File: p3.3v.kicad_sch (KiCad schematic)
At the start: 11 parts, among them U11 LT3045xDD

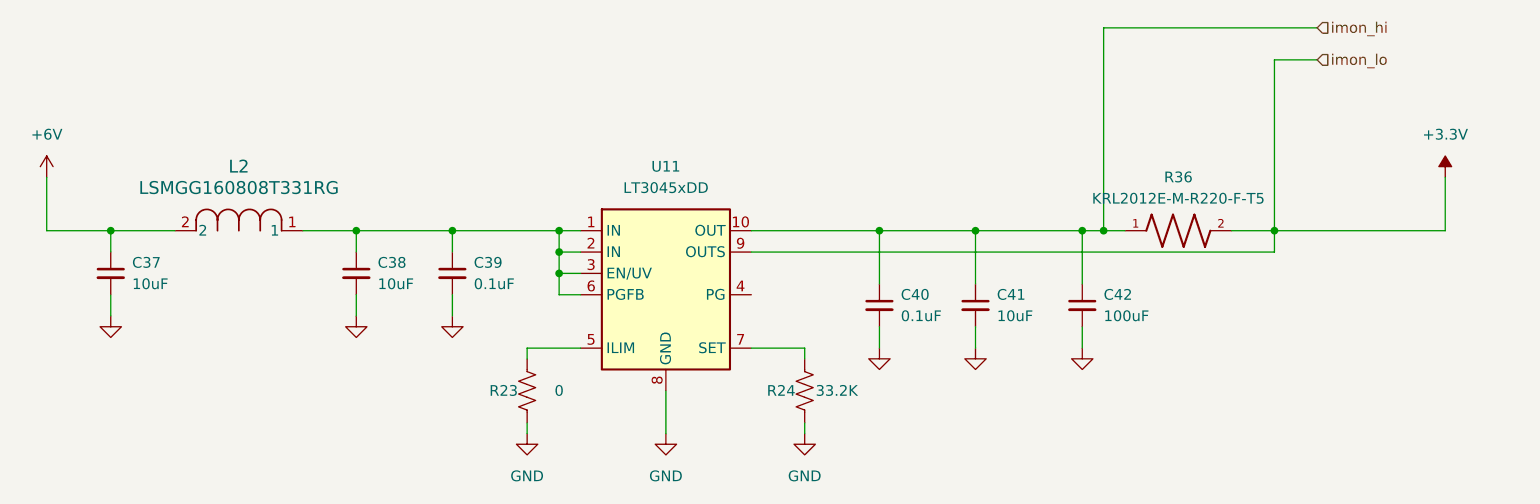
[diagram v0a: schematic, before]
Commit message: Add all 4 channels
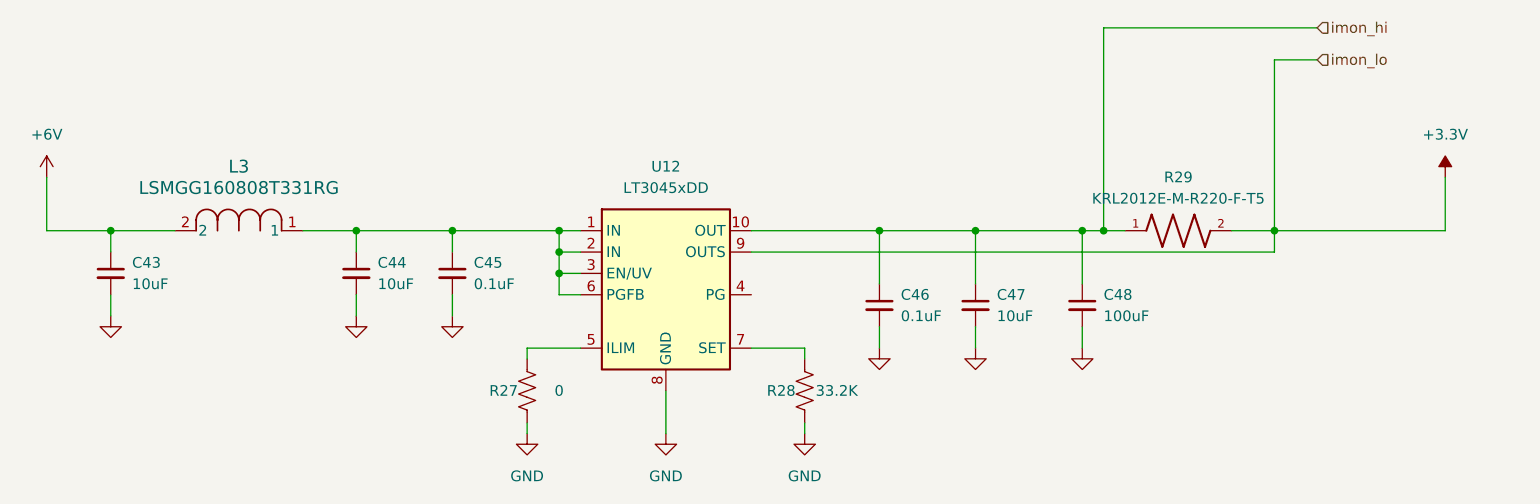
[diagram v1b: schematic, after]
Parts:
- renumbered C37 to C43, C38 to C44, C39 to C45, C40 to C46, C41 to C47, C42 to C48, L2 to L3, R23 to R27, R24 to R28, R36 to R29, U11 to U12
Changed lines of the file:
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@@
 		(dnp no)
 		(fields_autoplaced yes)
-		(property "Reference" "#PWR097"
+		(property "Reference" "#PWR0113"
 			(at 181.61 91.44 0)
 			(effects
@@
 			(project "psc_carrier_brd"
 				(path "/40891cc8-bf64-41f4-8f69-a607d7b280eb/d1842e08-6ad7-4891-bdb3-3a3a498e2a30/81cf0a5d-1890-4a8a-965e-c38ae4a2ca5e"
-					(reference "#PWR097")
+					(reference "#PWR0113")
 					(unit 1)
 				)
@@
 		(dnp no)
 		(fields_autoplaced yes)
-		(property "Reference" "#PWR099"
+		(property "Reference" "#PWR0115"
 			(at 237.49 68.58 0)
 			(effects
@@
 			(project ""
 				(path "/40891cc8-bf64-41f4-8f69-a607d7b280eb/d1842e08-6ad7-4891-bdb3-3a3a498e2a30/81cf0a5d-1890-4a8a-965e-c38ae4a2ca5e"
-					(reference "#PWR099")
+					(reference "#PWR0115")
 					(unit 1)
 				)
@@
 		(dnp no)
 		(fields_autoplaced yes)
-		(property "Reference" "#PWR090"
+		(property "Reference" "#PWR0106"
 			(at 78.74 87.63 0)
 			(effects
@@
 			(project "psc_carrier_brd"
 				(path "/40891cc8-bf64-41f4-8f69-a607d7b280eb/d1842e08-6ad7-4891-bdb3-3a3a498e2a30/81cf0a5d-1890-4a8a-965e-c38ae4a2ca5e"
-					(reference "#PWR090")
+					(reference "#PWR0106")
 					(unit 1)
 				)
@@
 		(on_board yes)
 		(dnp no)
-		(property "Reference" "R23"
+		(property "Reference" "R27"
 			(at 125.476 90.17 0)
 			(effects
@@
 			(project "psc_carrier_brd"
 				(path "/40891cc8-bf64-41f4-8f69-a607d7b280eb/d1842e08-6ad7-4891-bdb3-3a3a498e2a30/81cf0a5d-1890-4a8a-965e-c38ae4a2ca5e"
-					(reference "R23")
+					(reference "R27")
 					(unit 1)
 				)
@@
 		(on_board yes)
 		(dnp no)
-		(property "Reference" "C37"
+		(property "Reference" "C43"
 			(at 81.28 74.9362 0)
 			(effects
@@
 			(project "psc_carrier_brd"
 				(path "/40891cc8-bf64-41f4-8f69-a607d7b280eb/d1842e08-6ad7-4891-bdb3-3a3a498e2a30/81cf0a5d-1890-4a8a-965e-c38ae4a2ca5e"
-					(reference "C37")
+					(reference "C43")
 					(unit 1)
 				)
@@
 		(on_board yes)
 		(dnp no)
-		(property "Reference" "C39"
+		(property "Reference" "C45"
 			(at 121.92 74.9362 0)
 			(effects
@@
 			(project "psc_carrier_brd"
 				(path "/40891cc8-bf64-41f4-8f69-a607d7b280eb/d1842e08-6ad7-4891-bdb3-3a3a498e2a30/81cf0a5d-1890-4a8a-965e-c38ae4a2ca5e"
-					(reference "C39")
+					(reference "C45")
 					(unit 1)
 				)
@@
 		(dnp no)
 		(fields_autoplaced yes)
-		(property "Reference" "#PWR092"
+		(property "Reference" "#PWR0108"
 			(at 119.38 87.63 0)
 			(effects
@@
 			(project "psc_carrier_brd"
 				(path "/40891cc8-bf64-41f4-8f69-a607d7b280eb/d1842e08-6ad7-4891-bdb3-3a3a498e2a30/81cf0a5d-1890-4a8a-965e-c38ae4a2ca5e"
-					(reference "#PWR092")
+					(reference "#PWR0108")
 					(unit 1)
 				)
@@
 		(on_board yes)
 		(dnp no)
-		(property "Reference" "C42"
+		(property "Reference" "C48"
 			(at 196.85 78.7462 0)
 			(effects
@@
 			(project "psc_carrier_brd"
 				(path "/40891cc8-bf64-41f4-8f69-a607d7b280eb/d1842e08-6ad7-4891-bdb3-3a3a498e2a30/81cf0a5d-1890-4a8a-965e-c38ae4a2ca5e"
-					(reference "C42")
+					(reference "C48")
 					(unit 1)
 				)
@@
 		(on_board yes)
 		(dnp no)
-		(property "Reference" "R24"
+		(property "Reference" "R28"
 			(at 158.496 90.17 0)
 			(effects
@@
 			(project "psc_carrier_brd"
 				(path "/40891cc8-bf64-41f4-8f69-a607d7b280eb/d1842e08-6ad7-4891-bdb3-3a3a498e2a30/81cf0a5d-1890-4a8a-965e-c38ae4a2ca5e"
-					(reference "R24")
+					(reference "R28")
 					(unit 1)
 				)
@@
 		(dnp no)
 		(fields_autoplaced yes)
-		(property "Reference" "#PWR096"
+		(property "Reference" "#PWR0112"
 			(at 170.18 91.44 0)
 			(effects
@@
 			(project "psc_carrier_brd"
 				(path "/40891cc8-bf64-41f4-8f69-a607d7b280eb/d1842e08-6ad7-4891-bdb3-3a3a498e2a30/81cf0a5d-1890-4a8a-965e-c38ae4a2ca5e"
-					(reference "#PWR096")
+					(reference "#PWR0112")
 					(unit 1)
 				)
@@
 		(dnp no)
 		(fields_autoplaced yes)
-		(property "Reference" "#PWR095"
+		(property "Reference" "#PWR0111"
 			(at 161.29 101.6 0)
 			(effects
@@
 			(project "psc_carrier_brd"
 				(path "/40891cc8-bf64-41f4-8f69-a607d7b280eb/d1842e08-6ad7-4891-bdb3-3a3a498e2a30/81cf0a5d-1890-4a8a-965e-c38ae4a2ca5e"
-					(reference "#PWR095")
+					(reference "#PWR0111")
 					(unit 1)
 				)
@@
 		(dnp no)
 		(fields_autoplaced yes)
-		(property "Reference" "#PWR091"
+		(property "Reference" "#PWR0107"
 			(at 107.95 87.63 0)
 			(effects
@@
 			(project "psc_carrier_brd"
 				(path "/40891cc8-bf64-41f4-8f69-a607d7b280eb/d1842e08-6ad7-4891-bdb3-3a3a498e2a30/81cf0a5d-1890-4a8a-965e-c38ae4a2ca5e"
-					(reference "#PWR091")
+					(reference "#PWR0107")
 					(unit 1)
 				)
@@
 		(on_board yes)
 		(dnp no)
-		(property "Reference" "C38"
+		(property "Reference" "C44"
 			(at 110.49 74.9362 0)
 			(effects
@@
 			(project "psc_carrier_brd"
 				(path "/40891cc8-bf64-41f4-8f69-a607d7b280eb/d1842e08-6ad7-4891-bdb3-3a3a498e2a30/81cf0a5d-1890-4a8a-965e-c38ae4a2ca5e"
-					(reference "C38")
+					(reference "C44")
 					(unit 1)
 				)
@@
 		(dnp no)
 		(fields_autoplaced yes)
-		(property "Reference" "#PWR093"
+		(property "Reference" "#PWR0109"
 			(at 128.27 101.6 0)
 			(effects
@@
 			(project "psc_carrier_brd"
 				(path "/40891cc8-bf64-41f4-8f69-a607d7b280eb/d1842e08-6ad7-4891-bdb3-3a3a498e2a30/81cf0a5d-1890-4a8a-965e-c38ae4a2ca5e"
-					(reference "#PWR093")
+					(reference "#PWR0109")
 					(unit 1)
 				)
@@
 		(dnp no)
 		(fields_autoplaced yes)
-		(property "Reference" "R36"
+		(property "Reference" "R29"
 			(at 205.74 64.77 0)
 			(effects
@@
 			(project "psc_carrier_brd"
 				(path "/40891cc8-bf64-41f4-8f69-a607d7b280eb/d1842e08-6ad7-4891-bdb3-3a3a498e2a30/81cf0a5d-1890-4a8a-965e-c38ae4a2ca5e"
-					(reference "R36")
+					(reference "R29")
 					(unit 1)
 				)
@@
 		(dnp no)
 		(fields_autoplaced yes)
-		(property "Reference" "#PWR098"
+		(property "Reference" "#PWR0114"
 			(at 194.31 91.44 0)
 			(effects
@@
 			(project "psc_carrier_brd"
 				(path "/40891cc8-bf64-41f4-8f69-a607d7b280eb/d1842e08-6ad7-4891-bdb3-3a3a498e2a30/81cf0a5d-1890-4a8a-965e-c38ae4a2ca5e"
-					(reference "#PWR098")
+					(reference "#PWR0114")
 					(unit 1)
 				)
@@
 		(on_board yes)
 		(dnp no)
-		(property "Reference" "C40"
+		(property "Reference" "C46"
 			(at 172.72 78.7462 0)
 			(effects
@@
 			(project "psc_carrier_brd"
 				(path "/40891cc8-bf64-41f4-8f69-a607d7b280eb/d1842e08-6ad7-4891-bdb3-3a3a498e2a30/81cf0a5d-1890-4a8a-965e-c38ae4a2ca5e"
-					(reference "C40")
+					(reference "C46")
 					(unit 1)
 				)
@@
 		(dnp no)
 		(fields_autoplaced yes)
-		(property "Reference" "#PWR094"
+		(property "Reference" "#PWR0110"
 			(at 144.78 101.6 0)
 			(effects
@@
 			(project ""
 				(path "/40891cc8-bf64-41f4-8f69-a607d7b280eb/d1842e08-6ad7-4891-bdb3-3a3a498e2a30/81cf0a5d-1890-4a8a-965e-c38ae4a2ca5e"
-					(reference "#PWR094")
+					(reference "#PWR0110")
 					(unit 1)
 				)
@@
 		(dnp no)
 		(fields_autoplaced yes)
-		(property "Reference" "U11"
+		(property "Reference" "U12"
 			(at 144.78 63.5 0)
 			(effects
@@
 			(project ""
 				(path "/40891cc8-bf64-41f4-8f69-a607d7b280eb/d1842e08-6ad7-4891-bdb3-3a3a498e2a30/81cf0a5d-1890-4a8a-965e-c38ae4a2ca5e"
-					(reference "U11")
+					(reference "U12")
 					(unit 1)
 				)
@@
 		(on_board yes)
 		(dnp no)
-		(property "Reference" "C41"
+		(property "Reference" "C47"
 			(at 184.15 78.7462 0)
 			(effects
@@
 			(project "psc_carrier_brd"
 				(path "/40891cc8-bf64-41f4-8f69-a607d7b280eb/d1842e08-6ad7-4891-bdb3-3a3a498e2a30/81cf0a5d-1890-4a8a-965e-c38ae4a2ca5e"
-					(reference "C41")
+					(reference "C47")
 					(unit 1)
 				)
@@
 		(dnp no)
 		(fields_autoplaced yes)
-		(property "Reference" "L2"
+		(property "Reference" "L3"
 			(at 93.98 63.5 0)
 			(effects
@@
 			(project ""
 				(path "/40891cc8-bf64-41f4-8f69-a607d7b280eb/d1842e08-6ad7-4891-bdb3-3a3a498e2a30/81cf0a5d-1890-4a8a-965e-c38ae4a2ca5e"
-					(reference "L2")
+					(reference "L3")
 					(unit 1)
 				)
@@
 		(dnp no)
 		(fields_autoplaced yes)
-		(property "Reference" "#PWR089"
+		(property "Reference" "#PWR0105"
 			(at 71.12 68.58 0)
 			(effects
@@
 			(project ""
 				(path "/40891cc8-bf64-41f4-8f69-a607d7b280eb/d1842e08-6ad7-4891-bdb3-3a3a498e2a30/81cf0a5d-1890-4a8a-965e-c38ae4a2ca5e"
-					(reference "#PWR089")
-					(unit 1)
-				)
+					(reference "#PWR0105")
+					(unit 1)
+				)

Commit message: Start routing
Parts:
- renumbered C43 to C28, C44 to C29, C45 to C30, C46 to C31, C47 to C32, C48 to C33, R27 to R17, R28 to R18, R29 to R19, U12 to U8
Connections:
- net +6V renamed +5.0V
- no-connect marks 0 -> 1

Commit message: Finished layout
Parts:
- added TP5: ${SHORT_NET_NAME(1)}, TestPoint:TestPoint_THTPad_D2.0mm_Drill1.0mm, symbol Connector:TestPoint
- C28, C29, C32: Cost (none) -> .04; MFG (none) -> Samsung; MFG_PN (none) -> CL10A106MA8NRNC
- C30, C31: Cost (none) -> .01; MFG (none) -> Taiyo Yuden; MFG_PN (none) -> TMK105BJ104KV-F
- C33: Cost (none) -> 0.22; MFG (none) -> Murata; MFG_PN (none) -> GRM31CR61A107MEA8L
- L3: Cost (none) -> .01; MFG (none) -> Taiyo Yuden; MFG_PN (none) -> LSMGG160808T331RG
- R17: Cost (none) -> 0.01; MFG (none) -> Panasonic; MFG_PN (none) -> ERJ-2GE0R00X
- R18: Cost (none) -> 0.01; MFG (none) -> Panasonic; MFG_PN (none) -> ERJ-2RKF3322X
- R19: value KRL2012E-M-R220-F-T5 -> 0.22; Cost (none) -> 0.38; MFG (none) -> Susumu; MFG_PN (none) -> KRL2012E-M-R220-F-T5
- U8: Cost (none) -> 6.06; MFG (none) -> Analog Devices; MFG_PN (none) -> LT3045EDD#TRPBF
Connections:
- net +3.3V: now also TP5.1
- net Vin_3.3v: now reaches C29.1, C30.1, L3.1, U8.1 (IN), U8.2 (IN), U8.6 (PGFB)
- net Vin_3.3v: no longer U8.3 (EN/UV)
- new net enb: U8.3 (EN/UV)
